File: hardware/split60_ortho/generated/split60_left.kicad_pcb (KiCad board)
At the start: 2 copper layers, 181.1 x 143.3 mm, 65 parts

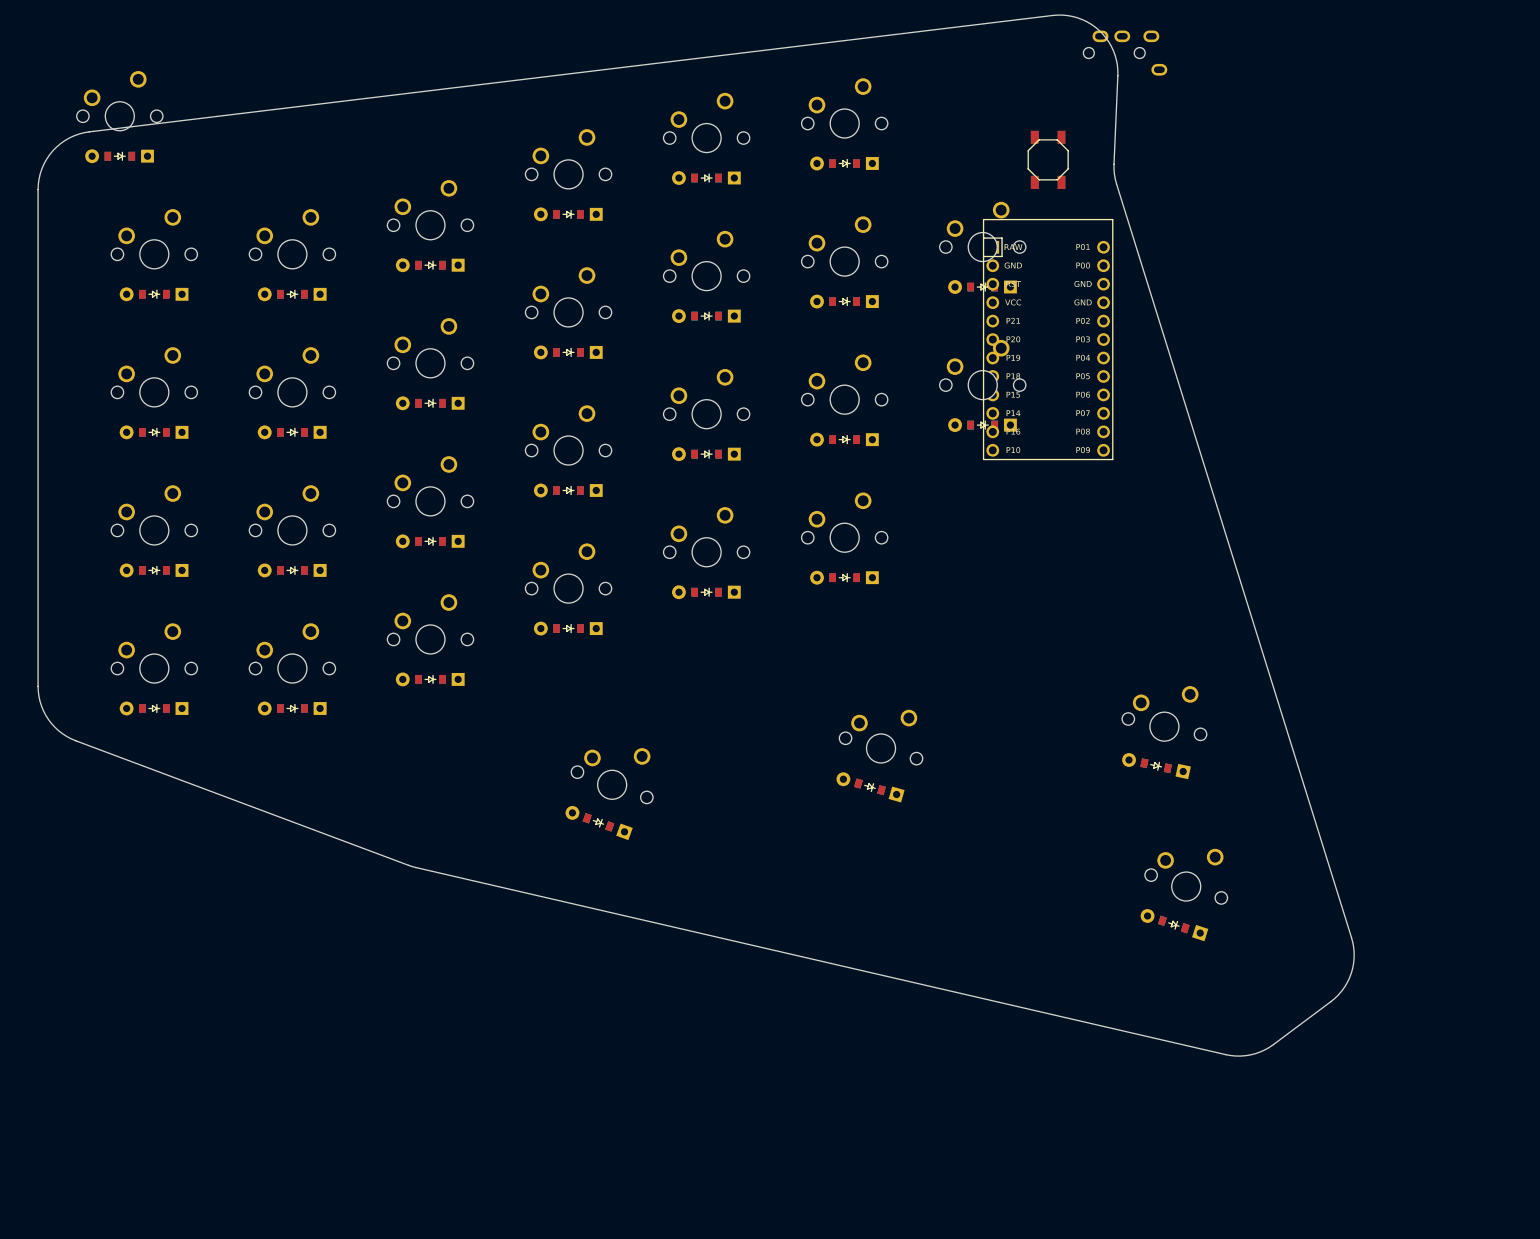
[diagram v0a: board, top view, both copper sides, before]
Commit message: Lower inner index columns
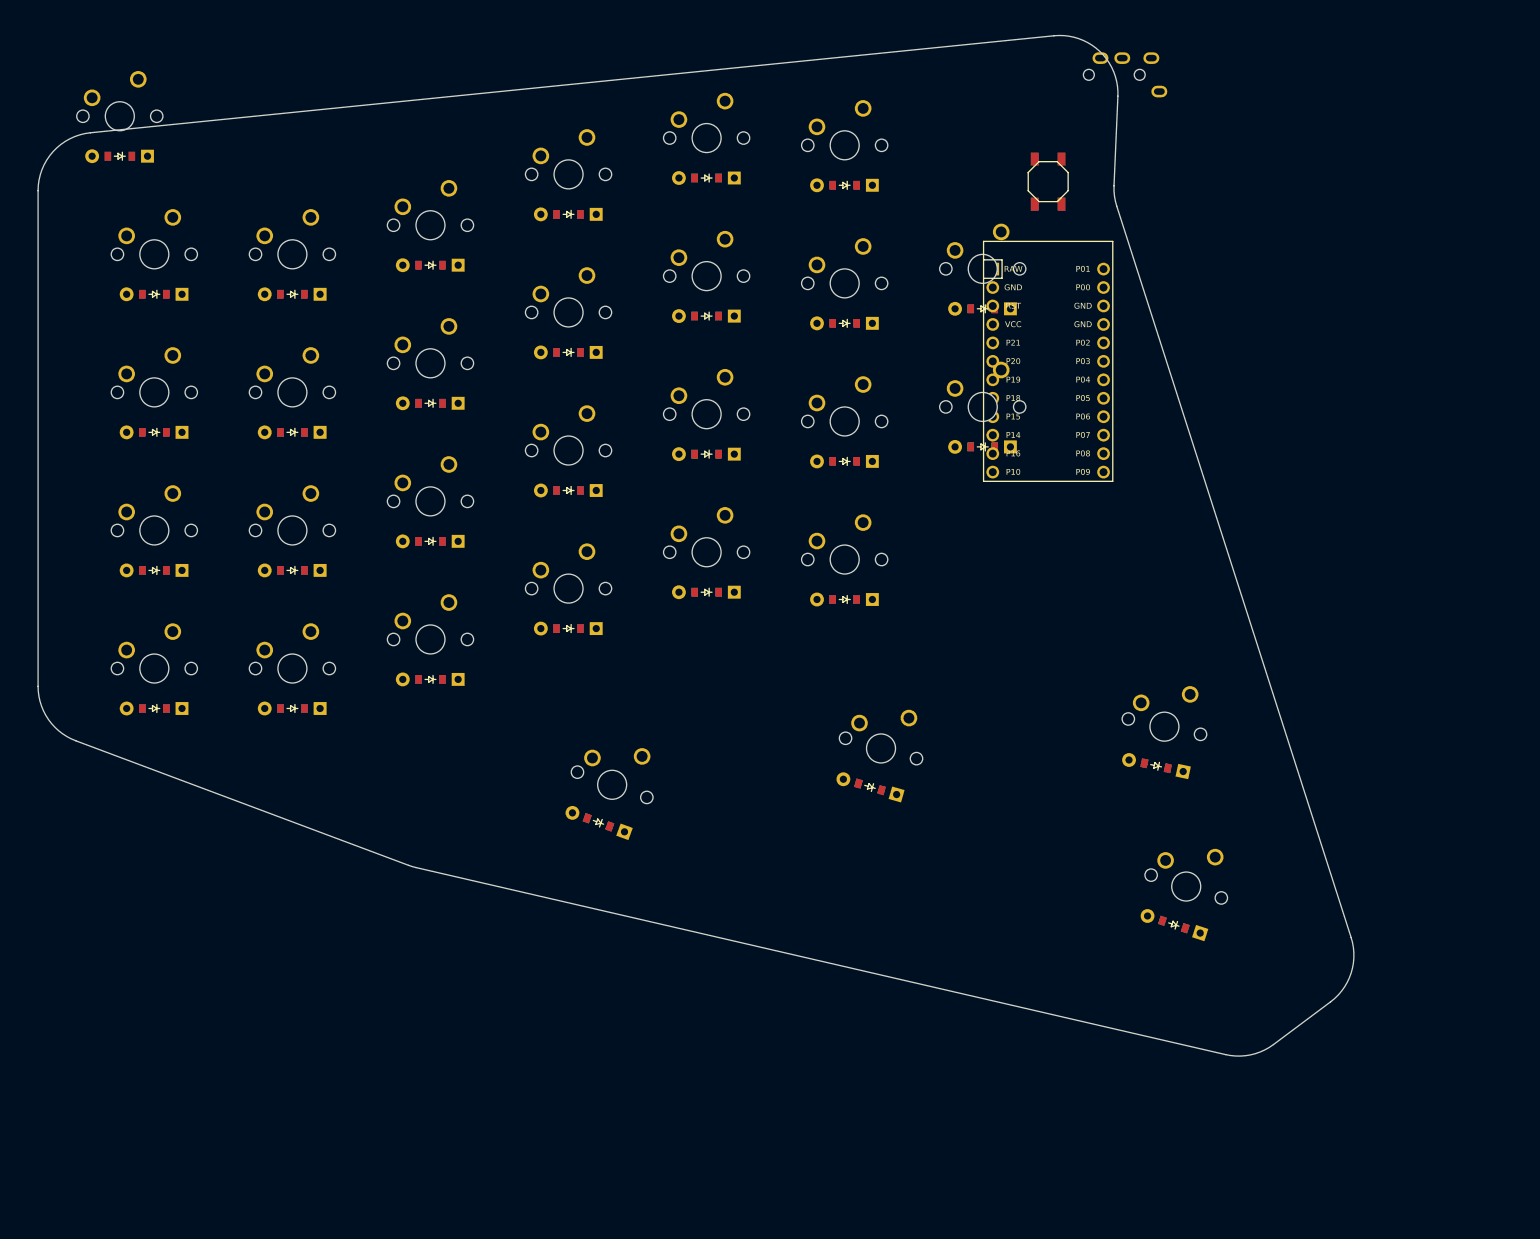
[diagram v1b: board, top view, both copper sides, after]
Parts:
- moved B1 3.00 mm to (123.0, -67.0)
- moved D22 3.00 mm to (95.0, -9.50)
- moved D23 3.00 mm to (95.0, -28.5)
- moved D24 3.00 mm to (95.0, -47.5)
- moved D25 3.00 mm to (95.0, -66.5)
- moved D26 3.00 mm to (114.0, -30.5)
- moved D27 3.00 mm to (114.0, -49.5)
- moved MCU1 3.00 mm to (123.0, -41.0)
- moved S22 3.00 mm to (95.0, -15.0)
- moved S23 3.00 mm to (95.0, -34.0)
- moved S24 3.00 mm to (95.0, -53.0)
- moved S25 3.00 mm to (95.0, -72.0)
- moved S26 3.00 mm to (114.0, -36.0)
- moved S27 3.00 mm to (114.0, -55.0)
- moved TRRS1 3.00 mm to (127.0, -84.0)
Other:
- board size 181.1 x 143.3 mm -> 181.1 x 140.4 mm
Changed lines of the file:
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@@
           )
       (module MX (layer F.Cu)
-      (at 95 -18 0)
+      (at 95 -15 0)
       (fp_text reference "S22" (at 0 0) (layer F.SilkS) hide (effects (font (size 1.27 1.27) (thickness 0.15))))
       (fp_text value "" (at 0 0) (layer F.SilkS) hide (effects (font (size 1.27 1.27) (thickness 0.15))))
@@
           )
       (module MX (layer F.Cu)
-      (at 95 -37 0)
+      (at 95 -34 0)
       (fp_text reference "S23" (at 0 0) (layer F.SilkS) hide (effects (font (size 1.27 1.27) (thickness 0.15))))
       (fp_text value "" (at 0 0) (layer F.SilkS) hide (effects (font (size 1.27 1.27) (thickness 0.15))))
@@
           )
       (module MX (layer F.Cu)
-      (at 95 -56 0)
+      (at 95 -53 0)
       (fp_text reference "S24" (at 0 0) (layer F.SilkS) hide (effects (font (size 1.27 1.27) (thickness 0.15))))
       (fp_text value "" (at 0 0) (layer F.SilkS) hide (effects (font (size 1.27 1.27) (thickness 0.15))))
@@
           )
       (module MX (layer F.Cu)
-      (at 95 -75 0)
+      (at 95 -72 0)
       (fp_text reference "S25" (at 0 0) (layer F.SilkS) hide (effects (font (size 1.27 1.27) (thickness 0.15))))
       (fp_text value "" (at 0 0) (layer F.SilkS) hide (effects (font (size 1.27 1.27) (thickness 0.15))))
@@
           )
       (module MX (layer F.Cu)
-      (at 114 -39 0)
+      (at 114 -36 0)
       (fp_text reference "S26" (at 0 0) (layer F.SilkS) hide (effects (font (size 1.27 1.27) (thickness 0.15))))
       (fp_text value "" (at 0 0) (layer F.SilkS) hide (effects (font (size 1.27 1.27) (thickness 0.15))))
@@
           )
       (module MX (layer F.Cu)
-      (at 114 -58 0)
+      (at 114 -55 0)
       (fp_text reference "S27" (at 0 0) (layer F.SilkS) hide (effects (font (size 1.27 1.27) (thickness 0.15))))
       (fp_text value "" (at 0 0) (layer F.SilkS) hide (effects (font (size 1.27 1.27) (thickness 0.15))))
@@
     )
     (module ComboDiode (layer F.Cu)
-        (at 95 -12.5 180)
+        (at 95 -9.5 180)
         (fp_text reference "D22" (at 0 0) (layer F.SilkS) hide (effects (font (size 1.27 1.27) (thickness 0.15))))
         (fp_text value "" (at 0 0) (layer F.SilkS) hide (effects (font (size 1.27 1.27) (thickness 0.15))))
@@
     )
     (module ComboDiode (layer F.Cu)
-        (at 95 -31.5 180)
+        (at 95 -28.5 180)
         (fp_text reference "D23" (at 0 0) (layer F.SilkS) hide (effects (font (size 1.27 1.27) (thickness 0.15))))
         (fp_text value "" (at 0 0) (layer F.SilkS) hide (effects (font (size 1.27 1.27) (thickness 0.15))))
@@
     )
     (module ComboDiode (layer F.Cu)
-        (at 95 -50.5 180)
+        (at 95 -47.5 180)
         (fp_text reference "D24" (at 0 0) (layer F.SilkS) hide (effects (font (size 1.27 1.27) (thickness 0.15))))
         (fp_text value "" (at 0 0) (layer F.SilkS) hide (effects (font (size 1.27 1.27) (thickness 0.15))))
@@
     )
     (module ComboDiode (layer F.Cu)
-        (at 95 -69.5 180)
+        (at 95 -66.5 180)
         (fp_text reference "D25" (at 0 0) (layer F.SilkS) hide (effects (font (size 1.27 1.27) (thickness 0.15))))
         (fp_text value "" (at 0 0) (layer F.SilkS) hide (effects (font (size 1.27 1.27) (thickness 0.15))))
@@
     )
     (module ComboDiode (layer F.Cu)
-        (at 114 -33.5 180)
+        (at 114 -30.5 180)
         (fp_text reference "D26" (at 0 0) (layer F.SilkS) hide (effects (font (size 1.27 1.27) (thickness 0.15))))
         (fp_text value "" (at 0 0) (layer F.SilkS) hide (effects (font (size 1.27 1.27) (thickness 0.15))))
@@
     )
     (module ComboDiode (layer F.Cu)
-        (at 114 -52.5 180)
+        (at 114 -49.5 180)
         (fp_text reference "D27" (at 0 0) (layer F.SilkS) hide (effects (font (size 1.27 1.27) (thickness 0.15))))
         (fp_text value "" (at 0 0) (layer F.SilkS) hide (effects (font (size 1.27 1.27) (thickness 0.15))))
@@
     )
       (module ProMicro (layer F.Cu)
-      (at 123 -44 -90)
+      (at 123 -41 -90)
       (fp_text reference "MCU1" (at 0 0) (layer F.SilkS) hide (effects (font (size 1.27 1.27) (thickness 0.15))))
       (fp_text value "" (at 0 0) (layer F.SilkS) hide (effects (font (size 1.27 1.27) (thickness 0.15))))
@@
         (descr "Low-profile SMD Tactile Switch, https://www.e-switch.com/product-catalog/tact/product-lines/tl3342-series-low-profile-smt-tact-switch")
         (tags "SPST Tactile Switch")
-        (at 123 -70 90)
+        (at 123 -67 90)
         (fp_text reference "B1" (at 0 0) (layer F.SilkS) hide (effects (font (size 1.27 1.27) (thickness 0.15))))
         (fp_text value "" (at 0 0) (layer F.SilkS) hide (effects (font (size 1.27 1.27) (thickness 0.15))))
@@
     )
       (module TRRS-PJ-320A-dual (layer F.Cu)
-      (at 127 -87 90)
+      (at 127 -84 90)
       (fp_text reference "TRRS1" (at 0 14.2) (layer Dwgs.User) (effects (font (size 1 1) (thickness 0.15))))
       (fp_text value TRRS-PJ-320A-dual (at 0 -5.6) (layer F.Fab) (effects (font (size 1 1) (thickness 0.15))))
@@
         (pad 4 thru_hole oval (at 0 3.2 90) (size 1.6 2.2) (drill oval 0.9 1.5) (layers *.Cu *.Mask) (net 44 "GND"))
       )
-  (gr_line (start -16 2.452165668523753) (end -16 -65.90827867583893) (angle 90) (layer Edge.Cuts) (width 0.15))
-(gr_line (start -8.959467234281922 -73.85053415961696) (end 123.63848894037348 -89.86907920085048) (angle 90) (layer Edge.Cuts) (width 0.15))
-(gr_line (start 132.5904054839006 -81.57932612971399) (end 132.0606625877834 -69.39523951901856) (angle 90) (layer Edge.Cuts) (width 0.15))
-(gr_line (start 132.41565251474495 -66.66673067483259) (end 164.75142578443067 37.055231966232554) (angle 90) (layer Edge.Cuts) (width 0.15))
-(gr_line (start 161.9030602535128 45.8444083594067) (end 154.00986634263845 51.743327385092186) (angle 90) (layer Edge.Cuts) (width 0.15))
+  (gr_line (start -16 2.452165668523753) (end -16 -65.76493264966443) (angle 90) (layer Edge.Cuts) (width 0.15))
+(gr_line (start -8.801319156122334 -73.72469941381318) (end 123.80479867550139 -87.07430859149343) (angle 90) (layer Edge.Cuts) (width 0.15))
+(gr_line (start 132.59856714086897 -78.76704423998626) (end 132.06208032136217 -66.42784739133003) (angle 90) (layer Edge.Cuts) (width 0.15))
+(gr_line (start 132.436149841043 -63.63897947140697) (end 164.6942024360189 37.02337933905238) (angle 90) (layer Edge.Cuts) (width 0.15))
+(gr_line (start 161.86491649782027 45.872914807963056) (end 154.00986634263845 51.743327385092186) (angle 90) (layer Edge.Cuts) (width 0.15))
 (gr_line (start 147.41993890647416 53.12983978294776) (end 35.99793152334434 27.387599684126613) (angle 90) (layer Edge.Cuts) (width 0.15))
 (gr_line (start 34.99462349182564 27.08537099352273) (end -10.804141616317114 9.944614512121838) (angle 90) (layer Edge.Cuts) (width 0.15))
-(gr_arc (start -8 -65.90827867583893) (end -8.9594672 -73.85053417583893) (angle -83.11174080678163) (layer Edge.Cuts) (width 0.15))
-(gr_arc (start 124.59795617465532 -81.92682371707245) (end 132.5904054746553 -81.57932611707245) (angle -99.37781062195506) (layer Edge.Cuts) (width 0.15))
-(gr_arc (start 140.0531118970287 -69.04774193166031) (end 132.0606625970287 -69.39523953166031) (angle -19.80464664019928) (layer Edge.Cuts) (width 0.15))
-(gr_arc (start 157.11396640214696 39.43624322306027) (end 161.90306020214695 45.84440832306027) (angle -70.5427723301642) (layer Edge.Cuts) (width 0.15))
+(gr_arc (start -8 -65.76493264966443) (end -8.8013192 -73.72469944966443) (angle -84.25133405754217) (layer Edge.Cuts) (width 0.15))
+(gr_arc (start 124.60611783162368 -79.11454182734468) (end 132.59856713162367 -78.76704422734468) (angle -98.23821737119434) (layer Edge.Cuts) (width 0.15))
+(gr_arc (start 140.05452963060745 -66.08034980397133) (end 132.06208033060744 -66.42784740397133) (angle -20.25802098026236) (layer Edge.Cuts) (width 0.15))
+(gr_arc (start 157.0758226464544 39.46474967161663) (end 161.8649164464544 45.87291477161663) (angle -70.99614667022291) (layer Edge.Cuts) (width 0.15))
 (gr_arc (start 149.2207724912726 45.33516224874579) (end 147.4199388912726 53.12983984874579) (angle -49.78132839635748) (layer Edge.Cuts) (width 0.15))
 (gr_arc (start 37.798765108142746 19.592922149924643) (end 34.994623508142745 27.085371049924643) (angle -7.509977851757441) (layer Edge.Cuts) (width 0.15))

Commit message: Refine column stagger and thumb outline
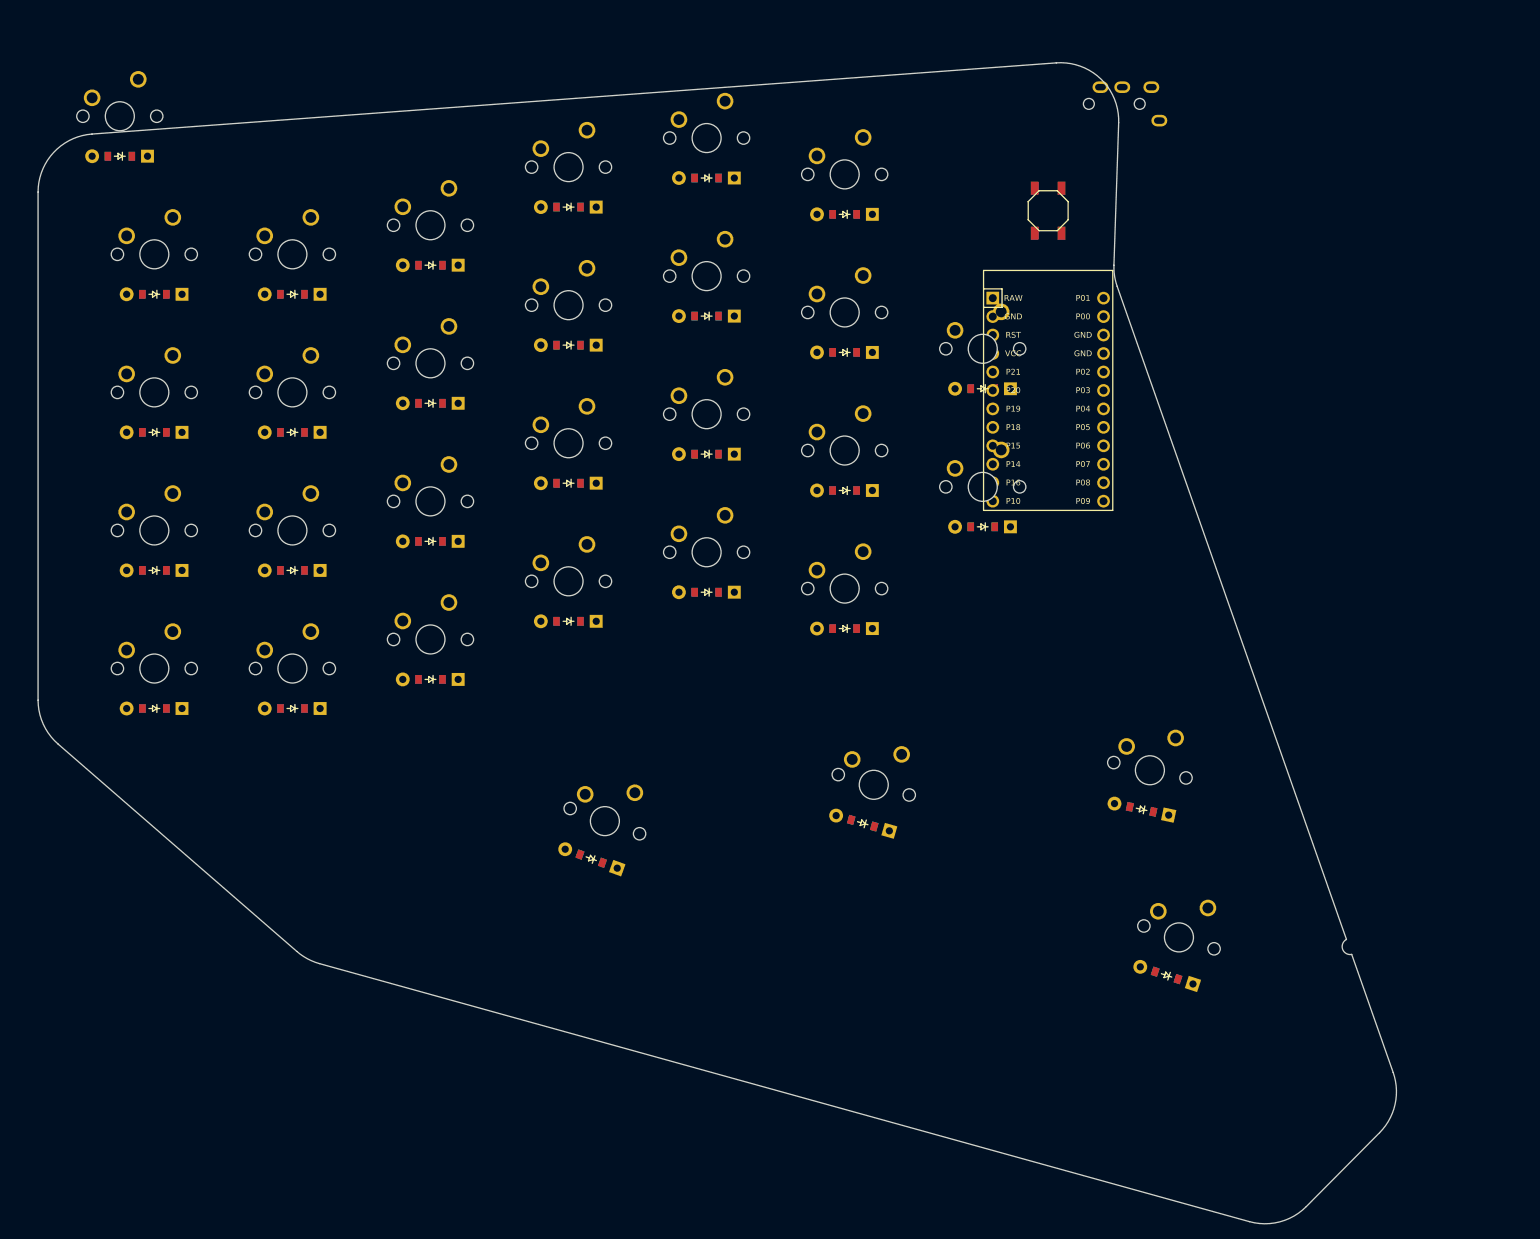
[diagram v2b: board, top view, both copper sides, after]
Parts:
- moved D26 11.0 mm to (114.0, -19.5)
- moved D27 11.0 mm to (114.0, -38.5)
- moved S26 11.0 mm to (114.0, -25.0)
- moved S27 11.0 mm to (114.0, -44.0)
- moved D31 7.07 mm to (139.3, 42.2)
- moved S31 7.07 mm to (141.0, 37.0)
- moved D30 6.32 mm to (135.9, 19.4)
- moved S30 6.32 mm to (137.0, 14.0)
- moved D28 5.10 mm to (60.1, 26.2)
- moved D29 5.10 mm to (97.5, 21.3)
- moved S28 5.10 mm to (62.0, 21.0)
- moved S29 5.10 mm to (99.0, 16.0)
- moved B1 4.00 mm to (123.0, -63.0)
- moved D22 4.00 mm to (95.0, -5.50)
- moved D23 4.00 mm to (95.0, -24.5)
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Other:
- board size 181.1 x 140.4 mm -> 186.9 x 159.8 mm
